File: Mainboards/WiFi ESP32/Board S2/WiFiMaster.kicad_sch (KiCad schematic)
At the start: 63 parts, among them IC1 MCP170X, IC2 NCP1117ST, IC3 ADuM142, IC4 ADuM142, IC5 ADuM142, IC6 IL0505, IC7 NCP1117ST, IC8 TPS61041, J1 USB_C_Receptacle_USB2.0, J2 Conn_02x05_Odd_Even, U1 ESP32-S3-MINI-1, X1 AKL18X-04W, X2 ALLSERIALMASTERM

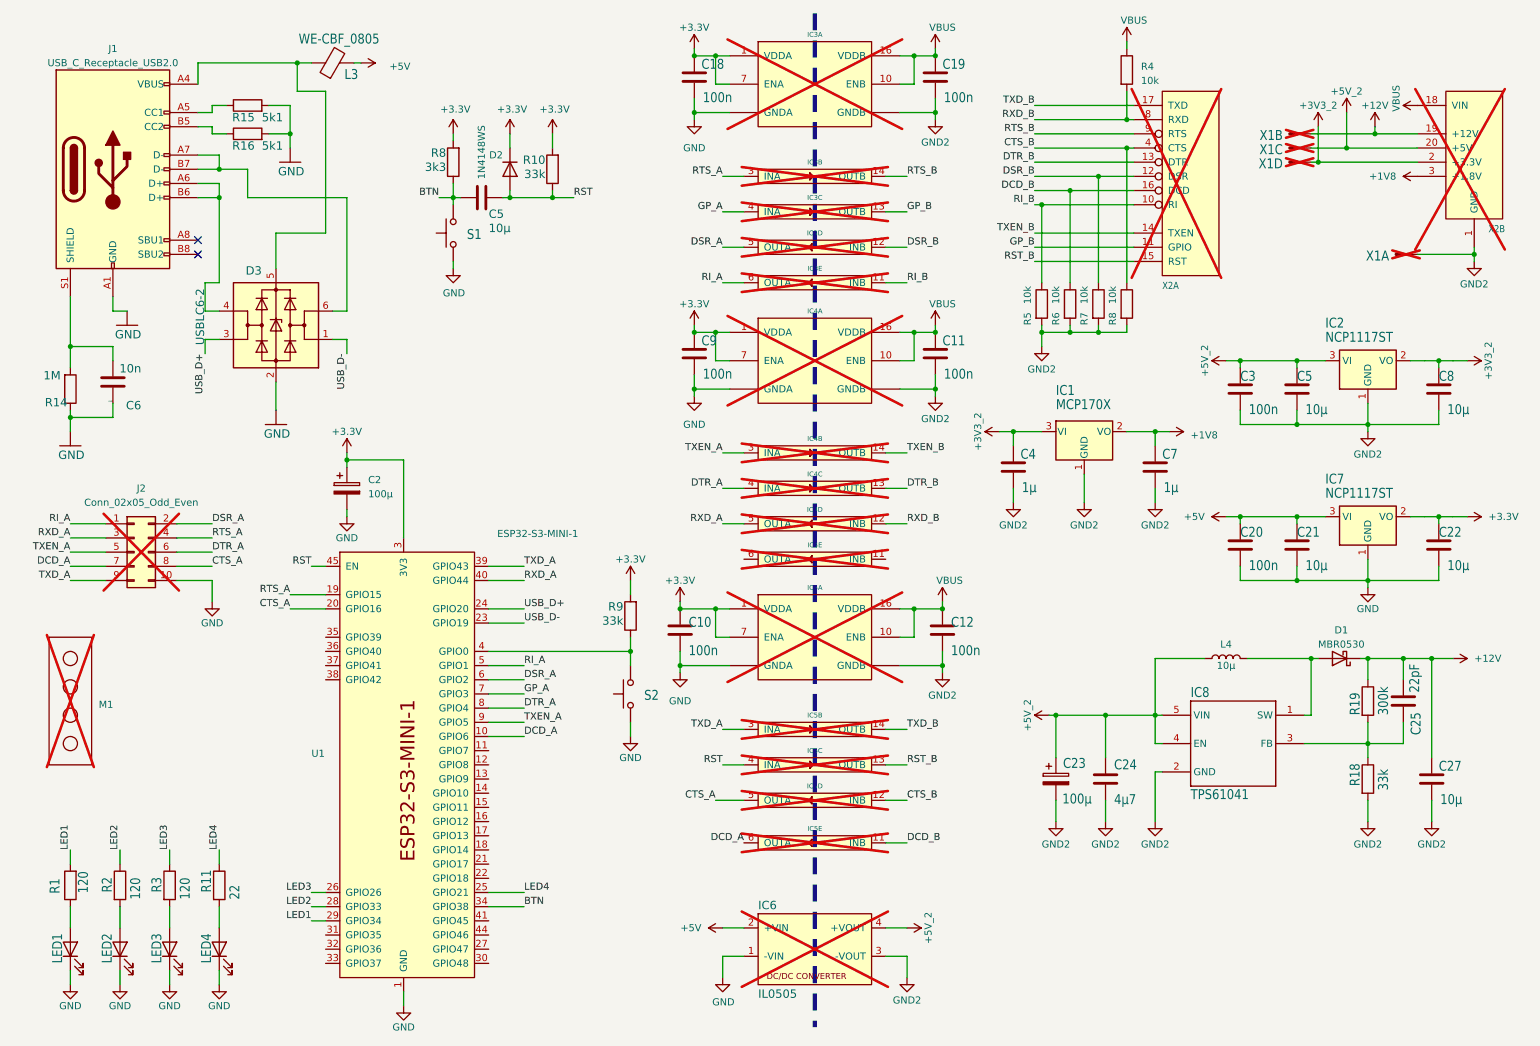
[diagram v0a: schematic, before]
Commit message: Update AllSerial libraries
update projects
add slave project template
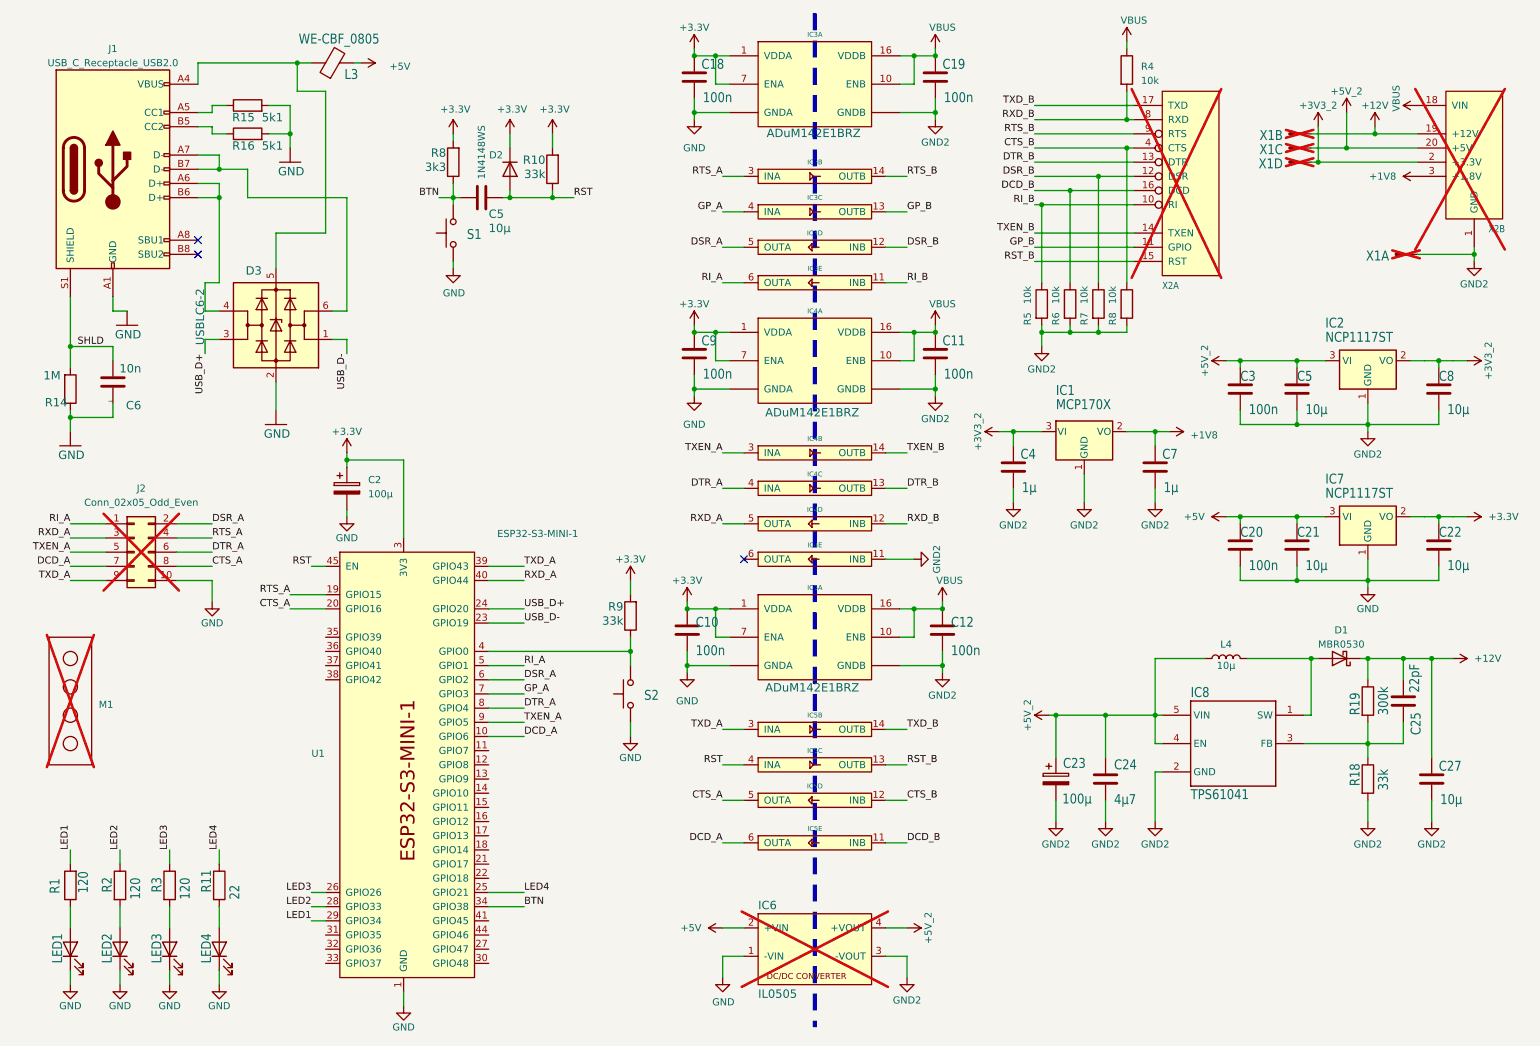
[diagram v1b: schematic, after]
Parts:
- IC3, IC4, IC5: value ADuM142 -> ADuM142E1BRZ; footprint Package_SO:SOP-16_3.9x9.9mm_P1.27mm -> Package_SO:SOIC-16_3.9x9.9mm_P1.27mm; now fitted
- J2: footprint Connector_IDC:IDC-Header_2x05_P2.54mm_Vertical -> Connector_PinHeader_2.54mm:PinHeader_2x05_P2.54mm_Vertical
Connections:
- net GND2: now also IC4.11 (INB)
- net SHLD: now reaches C6.1, J1.S1 (SHIELD), R14.2
- no-connect marks 2 -> 3
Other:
- moved on the sheet: C10

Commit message: improve board/front links
clean up
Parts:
- S2: footprint WiFiMaster:SWITCH_BZCN_TSB008 -> Button_Switch_SMD:SW_SPST_CK_RS282G05A3
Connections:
- net USB_D+: now also D3.1 (I/O1); no longer D3.3 (I/O2)
- net USB_D-: now also D3.3 (I/O2); no longer D3.1 (I/O1)
- net at J1.A6 (D+), J1.B6 (D+): now also D3.6 (I/O1); no longer D3.4 (I/O2)
- net at J1.A7 (D-), J1.B7 (D-): now also D3.4 (I/O2); no longer D3.6 (I/O1)
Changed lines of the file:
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@@
 	)
 	(junction
+		(at 48.26 45.72)
+		(diameter 0)
+		(color 0 0 0 0)
+	)
+	(junction
 		(at 273.05 55.88)
 		(diameter 0)
@@
 	)
 	(junction
-		(at 48.26 45.72)
-		(diameter 0)
-		(color 0 0 0 0)
-	)
-	(junction
 		(at 177.8 119.38)
 		(diameter 0)
@@
 	(wire
 		(pts
-			(xy 44.45 45.72) (xy 48.26 45.72)
+			(xy 66.04 26.67) (xy 66.04 44.45)
 		)
 		(stroke
@@
 	(wire
 		(pts
-			(xy 21.59 72.39) (xy 21.59 76.2)
+			(xy 44.45 45.72) (xy 48.26 45.72)
 		)
 		(stroke
@@
 	(wire
 		(pts
-			(xy 241.3 74.93) (xy 241.3 76.2)
+			(xy 21.59 72.39) (xy 21.59 76.2)
 		)
 		(stroke
@@
 	(wire
 		(pts
-			(xy 254 143.51) (xy 260.35 143.51)
+			(xy 241.3 74.93) (xy 241.3 76.2)
 		)
 		(stroke
@@
 	(wire
 		(pts
-			(xy 45.72 60.96) (xy 45.72 66.04)
+			(xy 254 143.51) (xy 260.35 143.51)
 		)
 		(stroke
@@
 	(wire
 		(pts
-			(xy 53.34 45.72) (xy 71.12 45.72)
-		)
-		(stroke
-			(width 0)
-			(type default)
-		)
-	)
-	(wire
-		(pts
 			(xy 96.52 121.92) (xy 102.87 121.92)
 		)
@@
 	(wire
 		(pts
+			(xy 48.26 45.72) (xy 48.26 49.53)
+		)
+		(stroke
+			(width 0)
+			(type default)
+		)
+	)
+	(wire
+		(pts
 			(xy 266.7 111.76) (xy 266.7 114.3)
 		)
@@
 	(wire
 		(pts
-			(xy 67.31 52.07) (xy 67.31 26.67)
-		)
-		(stroke
-			(width 0)
-			(type default)
-		)
-	)
-	(wire
-		(pts
 			(xy 210.82 36.83) (xy 212.09 36.83)
 		)
@@
 	(wire
 		(pts
-			(xy 71.12 71.12) (xy 71.12 73.66)
+			(xy 71.12 52.07) (xy 73.66 52.07)
 		)
 		(stroke
@@
 	(wire
 		(pts
-			(xy 58.42 78.74) (xy 58.42 83.82)
+			(xy 66.04 57.15) (xy 66.04 58.42)
 		)
 		(stroke
@@
 	(wire
 		(pts
-			(xy 53.34 40.64) (xy 53.34 45.72)
-		)
-		(stroke
-			(width 0)
-			(type default)
-		)
-	)
-	(wire
-		(pts
-			(xy 48.26 45.72) (xy 48.26 60.96)
-		)
-		(stroke
-			(width 0)
-			(type default)
-		)
-	)
-	(wire
-		(pts
 			(xy 90.17 45.72) (xy 90.17 46.99)
 		)
@@
 	(wire
 		(pts
-			(xy 71.12 45.72) (xy 71.12 66.04)
-		)
-		(stroke
-			(width 0)
-			(type default)
-		)
-	)
-	(wire
-		(pts
 			(xy 241.3 102.87) (xy 241.3 104.14)
 		)
@@
 	(wire
 		(pts
+			(xy 53.34 52.07) (xy 53.34 40.64)
+		)
+		(stroke
+			(width 0)
+			(type default)
+		)
+	)
+	(wire
+		(pts
 			(xy 241.3 114.3) (xy 254 114.3)
 		)
@@
 	(wire
 		(pts
+			(xy 60.96 52.07) (xy 53.34 52.07)
+		)
+		(stroke
+			(width 0)
+			(type default)
+		)
+	)
+	(wire
+		(pts
 			(xy 177.8 129.54) (xy 177.8 127)
 		)
@@
 	(wire
 		(pts
-			(xy 58.42 52.07) (xy 67.31 52.07)
+			(xy 40.64 114.3) (xy 46.99 114.3)
 		)
 		(stroke
@@
 	(wire
 		(pts
-			(xy 40.64 114.3) (xy 46.99 114.3)
+			(xy 205.74 68.58) (xy 205.74 69.85)
 		)
 		(stroke
@@
 	(wire
 		(pts
-			(xy 205.74 68.58) (xy 205.74 69.85)
+			(xy 198.12 153.67) (xy 198.12 157.48)
 		)
 		(stroke
@@
 	(wire
 		(pts
-			(xy 198.12 153.67) (xy 198.12 157.48)
+			(xy 44.45 43.18) (xy 48.26 43.18)
 		)
 		(stroke
@@
 	(wire
 		(pts
-			(xy 44.45 43.18) (xy 48.26 43.18)
+			(xy 176.53 80.01) (xy 176.53 81.28)
 		)
 		(stroke
@@
 	(wire
 		(pts
-			(xy 176.53 80.01) (xy 176.53 81.28)
+			(xy 137.16 119.38) (xy 139.7 119.38)
 		)
 		(stroke
@@
 	(wire
 		(pts
-			(xy 137.16 119.38) (xy 139.7 119.38)
+			(xy 64.77 170.18) (xy 67.31 170.18)
 		)
 		(stroke
@@
 	(wire
 		(pts
-			(xy 64.77 170.18) (xy 67.31 170.18)
+			(xy 48.26 49.53) (xy 60.96 49.53)
 		)
 		(stroke
@@
 	(wire
 		(pts
-			(xy 58.42 58.42) (xy 58.42 52.07)
-		)
-		(stroke
-			(width 0)
-			(type default)
-		)
-	)
-	(wire
-		(pts
 			(xy 266.7 102.87) (xy 269.24 102.87)
 		)
@@
 	(wire
 		(pts
-			(xy 68.58 71.12) (xy 71.12 71.12)
-		)
-		(stroke
-			(width 0)
-			(type default)
-		)
-	)
-	(wire
-		(pts
 			(xy 172.72 20.32) (xy 170.18 20.32)
 		)
@@
 	(wire
 		(pts
-			(xy 67.31 26.67) (xy 62.23 26.67)
+			(xy 66.04 26.67) (xy 62.23 26.67)
 		)
 		(stroke
@@
 	(wire
 		(pts
-			(xy 45.72 66.04) (xy 48.26 66.04)
-		)
-		(stroke
-			(width 0)
-			(type default)
-		)
-	)
-	(wire
-		(pts
 			(xy 44.45 30.48) (xy 46.99 30.48)
 		)
@@
 	(wire
 		(pts
-			(xy 48.26 71.12) (xy 45.72 71.12)
-		)
-		(stroke
-			(width 0)
-			(type default)
-		)
-	)
-	(wire
-		(pts
 			(xy 27.94 104.14) (xy 21.59 104.14)
 		)
@@
 	(wire
 		(pts
-			(xy 71.12 66.04) (xy 68.58 66.04)
-		)
-		(stroke
-			(width 0)
-			(type default)
-		)
-	)
-	(wire
-		(pts
-			(xy 45.72 71.12) (xy 45.72 73.66)
+			(xy 71.12 49.53) (xy 73.66 49.53)
 		)
 		(stroke
@@
 	(wire
 		(pts
-			(xy 48.26 60.96) (xy 45.72 60.96)
-		)
-		(stroke
-			(width 0)
-			(type default)
-		)
-	)
-	(wire
-		(pts
 			(xy 138.43 176.53) (xy 142.24 176.53)
 		)
@@
 	)
 	(label "USB_D-"
-		(at 71.12 73.66 270)
+		(at 73.66 52.07 0)
 		(fields_autoplaced yes)
 		(effects
@@
 				(size 1.27 1.27)
 			)
-			(justify right bottom)
+			(justify left bottom)
 		)
 	)
@@
 	)
 	(label "USB_D+"
-		(at 45.72 73.66 270)
+		(at 73.66 49.53 0)
 		(fields_autoplaced yes)
 		(effects
@@
 				(size 1.27 1.27)
 			)
-			(justify right bottom)
+			(justify left bottom)
 		)
 	)
@@
 	(symbol
 		(lib_id "FTDI_master-eagle-import:GND")
-		(at 58.42 86.36 0)
+		(at 66.04 60.96 0)
 		(mirror y)
 		(unit 1)
@@
 		(dnp no)
 		(property "Reference" "#GND04"
-			(at 58.42 86.36 0)
+			(at 66.04 60.96 0)
 			(effects
 				(font
@@
 		)
 		(property "Value" "GND"
-			(at 60.96 88.9 0)
+			(at 68.58 63.5 0)
 			(effects
 				(font
@@
 		)
 		(property "Footprint" ""
-			(at 58.42 86.36 0)
+			(at 66.04 60.96 0)
 			(effects
 				(font
@@
 		)
 		(property "Datasheet" ""
-			(at 58.42 86.36 0)
+			(at 66.04 60.96 0)
 			(effects
 				(font
@@
 		)
 		(property "Description" ""
-			(at 58.42 86.36 0)
+			(at 66.04 60.96 0)
 			(effects
 				(font
@@
 	(symbol
 		(lib_id "Power_Protection:USBLC6-2SC6")
-		(at 58.42 68.58 0)
+		(at 66.04 49.53 0)
 		(mirror y)
 		(unit 1)
@@
 		(dnp no)
 		(property "Reference" "D3"
-			(at 55.88 59.69 0)
+			(at 64.262 45.72 0)
 			(effects
 				(font
@@
 		)
 		(property "Value" "USBLC6-2"
-			(at 45.72 61.976 90)
+			(at 68.58 33.782 90)
 			(effects
 				(font
@@
 		)
 		(property "Footprint" "Package_TO_SOT_SMD:SOT-23-6"
-			(at 58.42 68.58 0)
+			(at 64.77 55.88 0)
 			(effects
 				(font
 					(size 1.27 1.27)
+					(italic yes)
 				)
+				(justify left)
 				(hide yes)
 			)
 		)
-		(property "Datasheet" ""
-			(at 58.42 68.58 0)
+		(property "Datasheet" "https://www.st.com/resource/en/datasheet/usblc6-2.pdf"
+			(at 64.77 57.785 0)
 			(effects
 				(font
 					(size 1.27 1.27)
 				)
+				(justify left)
 				(hide yes)
 			)
 		)
 		(property "Description" "Very low capacitance ESD protection diode, 2 data-line, SOT-23-6"
-			(at 58.42 68.58 0)
+			(at 66.04 49.53 0)
 			(effects
 				(font
@@
 		)
 		(property "LCSC" "C5197386"
-			(at 58.42 68.58 0)
+			(at 66.04 49.53 0)
 			(effects
 				(font
@@
 			)
 		)
-		(property "Footprint" "WiFiMaster:SWITCH_BZCN_TSB008"
+		(property "Footprint" "Button_Switch_SMD:SW_SPST_CK_RS282G05A3"
 			(at 116.84 134.62 0)
 			(effects

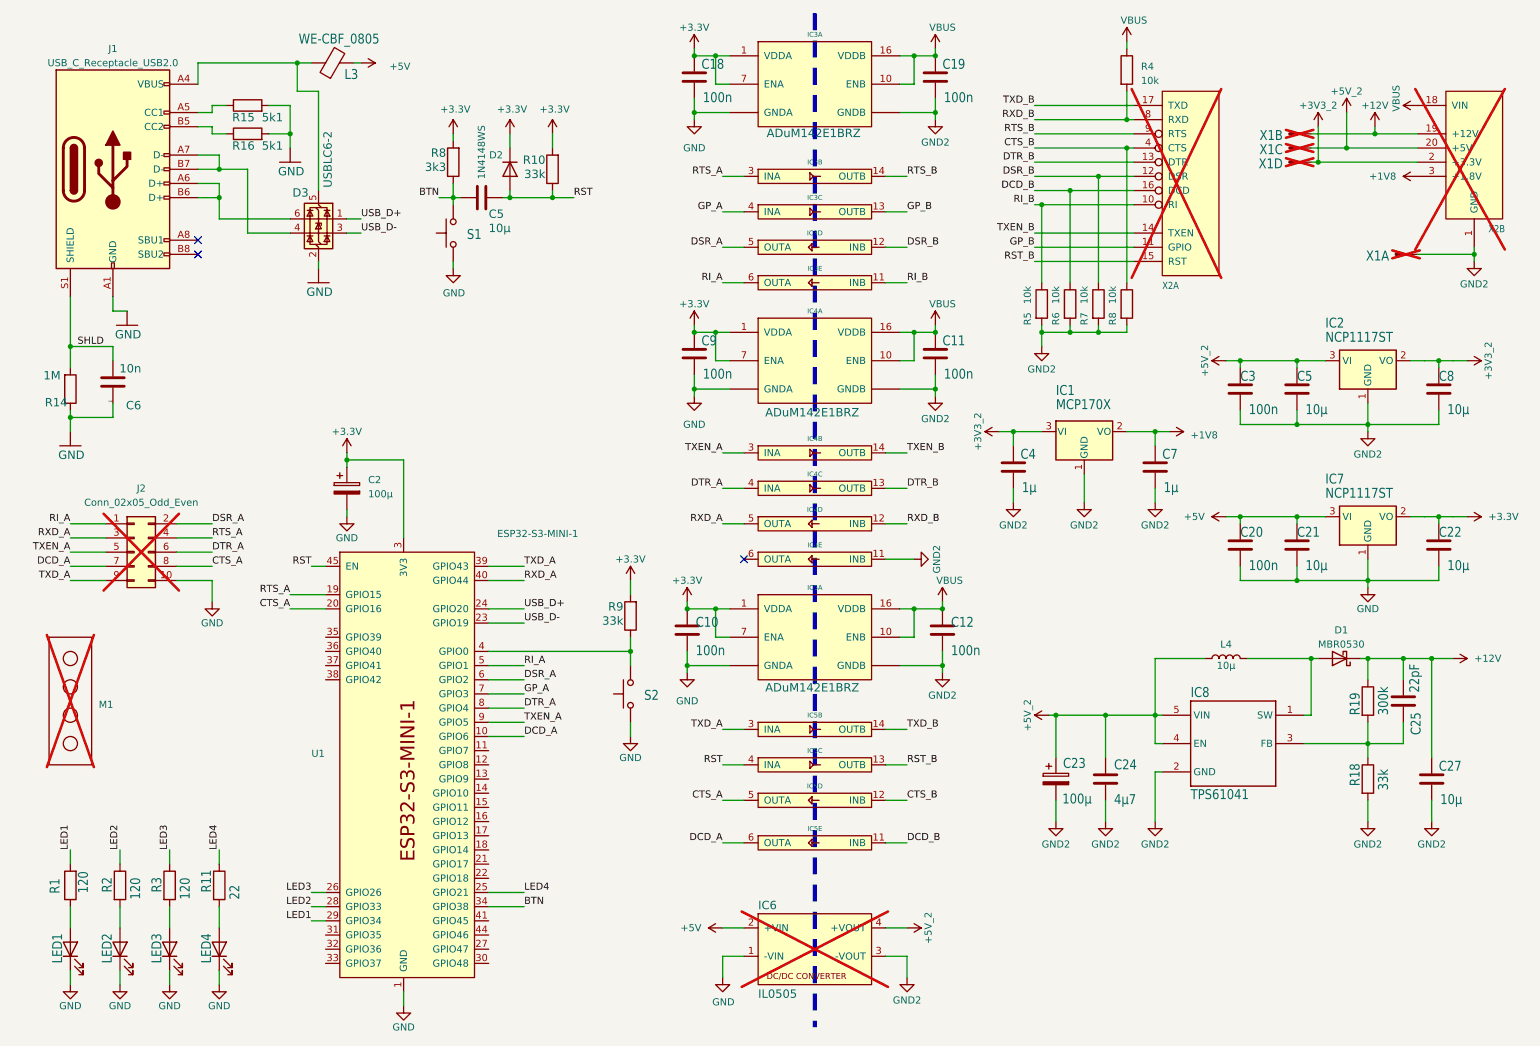
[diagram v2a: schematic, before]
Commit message: Migrate to KiCad 9
Add eBus board
Add various libraries
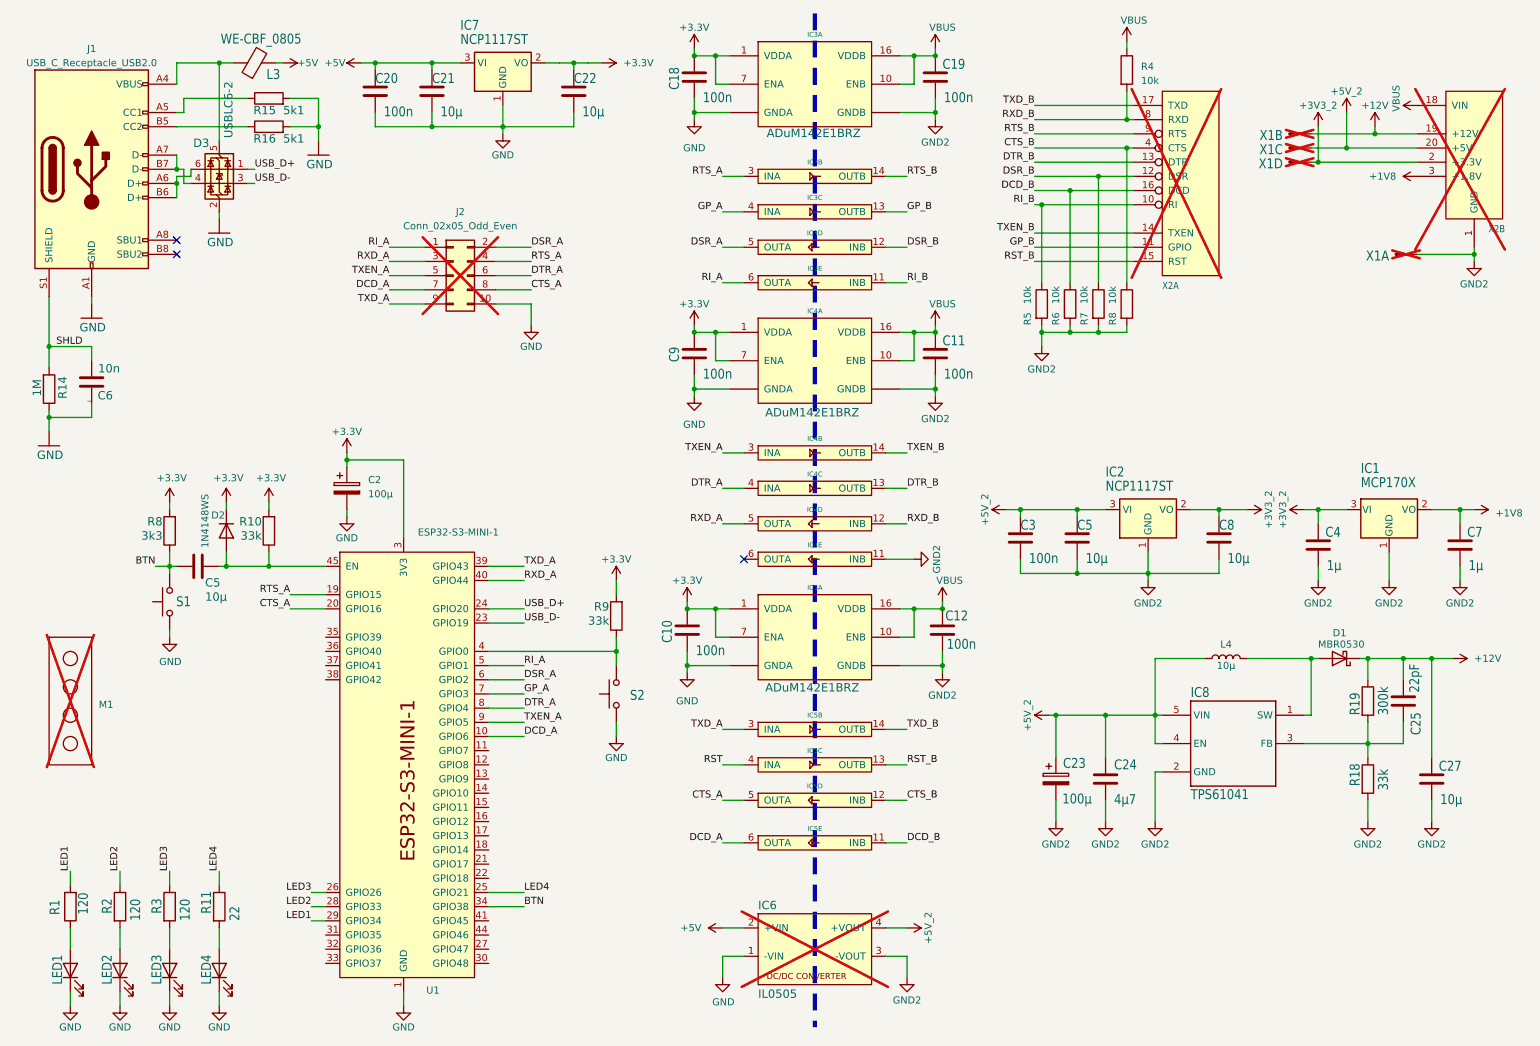
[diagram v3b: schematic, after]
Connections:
- net RST: no longer C5.1, D2.2 (A), R10.1, U1.45 (EN)
- new net: C5.1, D2.2 (A), R10.1, U1.45 (EN)
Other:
- moved on the sheet: C20, C21, C22, C3, C4, C5, C6, C7, C8, D2, D3, IC1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
